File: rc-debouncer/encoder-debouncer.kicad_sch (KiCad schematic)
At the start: 28 parts, among them J1 MCU, J2 SIG.IN, SW1 Input, U1 LM311, U2 LM358

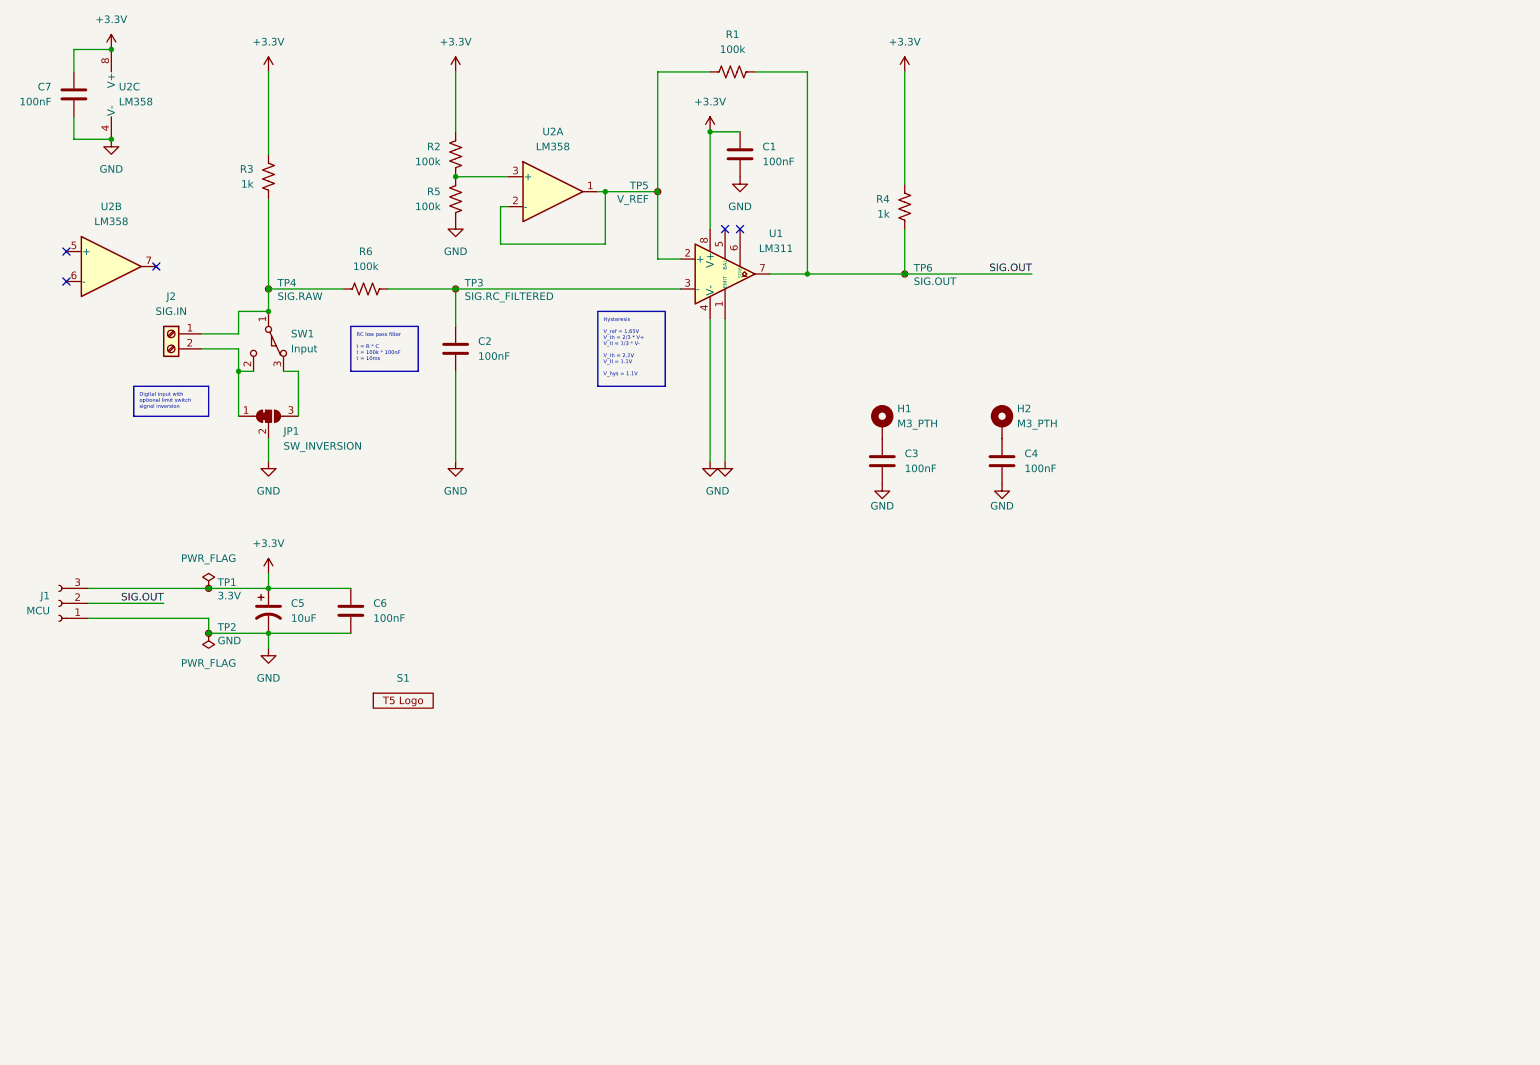
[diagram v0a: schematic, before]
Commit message: Finish new layout
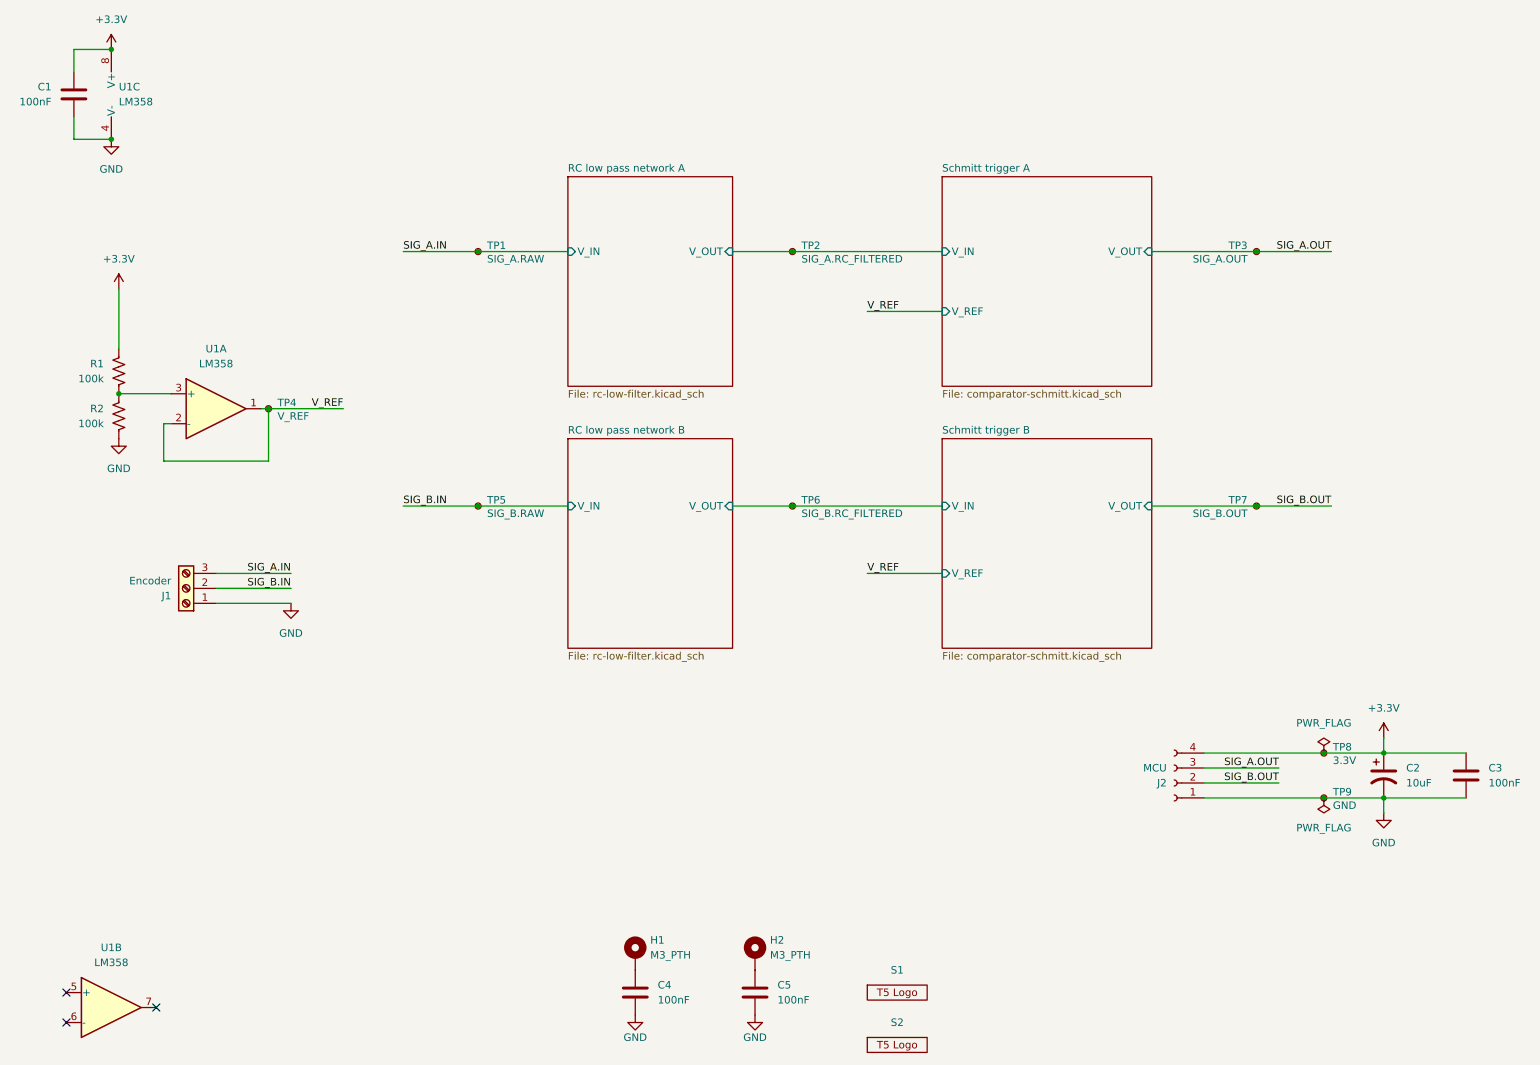
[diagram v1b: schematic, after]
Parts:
- removed C1, C2: 100nF, Capacitor_THT:C_Disc_D3.0mm_W2.0mm_P2.50mm, symbol GS_Capacitor_THT:C_THT_Ceramic_Disk
- removed J2: SIG.IN, TerminalBlock:TerminalBlock_Xinya_XY308-2.54-2P_1x02_P2.54mm_Horizontal, symbol GS_Connectors:Screw_Terminal_01x02_2.54mm_Xinya
- removed JP1: SW_INVERSION, Jumper:SolderJumper-3_P1.3mm_Bridged12_RoundedPad1.0x1.5mm, symbol Jumper:SolderJumper_3_Bridged12
- removed R1, R6: 100k, Resistor_THT:R_Axial_DIN0309_L9.0mm_D3.2mm_P12.70mm_Horizontal, symbol GS_Resistor_THT:R_250mW
- removed R3, R4: 1k, Resistor_THT:R_Axial_DIN0309_L9.0mm_D3.2mm_P12.70mm_Horizontal, symbol GS_Resistor_THT:R_250mW
- removed SW1: Input, Button_Switch_THT:SW_XKB_DM1-16UP-1, symbol GS_Switches:SW_SPDT_XKB_WK1-X-TIAIHUA
- removed U1: LM311, Package_DIP:DIP-8_W7.62mm_LongPads, symbol GS_Comparators:LM311
- removed unit 1 of U2
- added J1: Encoder, TerminalBlock:TerminalBlock_Xinya_XY308-2.54-3P_1x03_P2.54mm_Horizontal, symbol Connector:Screw_Terminal_01x03
- added S2: Logo, GS_Virtual:ENPH253_Logo, symbol GS_Virtual:ENPH253_Logo
- added TP5: SIG_B.RAW, TestPoint:TestPoint_Pad_1.5x1.5mm, symbol Connector:TestPoint_Small
- added TP6: SIG_B.RC_FILTERED, TestPoint:TestPoint_Pad_1.5x1.5mm, symbol Connector:TestPoint_Small
- added TP7: SIG_B.OUT, TestPoint:TestPoint_Pad_1.5x1.5mm, symbol Connector:TestPoint_Small
- added unit 1 of U1
- C4: renamed from C3; symbol GS_Capacitor_THT:C_THT_100nF -> GS_Capacitor_THT:C_THT_Ceramic_Disk
- C5: renamed from C4; symbol GS_Capacitor_THT:C_THT_100nF -> GS_Capacitor_THT:C_THT_Ceramic_Disk
- J2: renamed from J1; footprint GS_Connectors:JST_XH_S3B-XH-A-1_1x03_P2.50mm_Horizontal -> GS_Connectors:JST_XH_S4B-XH-A-1_1x04_P2.50mm_Horizontal; symbol Connector:Conn_01x03_Socket -> Connector:Conn_01x04_Socket
- S1: footprint GS_Virtual:ENPH253_Logo -> GS_Virtual:ENPH253_Logo_Small
- TP1: renamed from TP4; value SIG.RAW -> SIG_A.RAW
- TP2: renamed from TP3; value SIG.RC_FILTERED -> SIG_A.RC_FILTERED
- TP3: renamed from TP6; value SIG.OUT -> SIG_A.OUT
- renumbered C7 to C1, C5 to C2, C6 to C3, R2 to R1, R5 to R2, TP5 to TP4, TP1 to TP8, TP2 to TP9, U2 to U1
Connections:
- net +3.3V: now also J2.4 (Pin_4); no longer J2.3 (Pin_3)
- net GND: now also J1.1 (Pin_1)
- net SIG_A.IN: now reaches TP1.1
- net SIG_A.IN: now also J1.3 (Pin_3)
- net RC low pass network A/V_OUT: now reaches TP2.1
- net V_REF: now reaches TP4.1
- net V_REF: now also U1.1, U1.2 (-)
- net at R1.1, R2.2: now also U1.3 (+)
- net SIG.OUT renamed SIG_A.OUT
- net SIG_A.OUT: now also J2.3 (Pin_3); no longer J2.2 (Pin_2)
- new net RC low pass network B/V_OUT: TP6.1
- new net SIG_B.IN: J1.2 (Pin_2), TP5.1
- new net SIG_B.OUT: J2.2 (Pin_2), TP7.1
- no-connect marks 5 -> 3
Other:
- added sheet RC low pass network A (rc-low-filter.kicad_sch)
- added sheet RC low pass network B (rc-low-filter.kicad_sch)
- added sheet Schmitt trigger A (comparator-schmitt.kicad_sch)
- added sheet Schmitt trigger B (comparator-schmitt.kicad_sch)
- title: RC Debouncer -> Encoder Debouncer
- moved on the sheet: C2, C3, C4, C5, H1, H2, R1, R2, S1, TP1, TP2, TP3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
